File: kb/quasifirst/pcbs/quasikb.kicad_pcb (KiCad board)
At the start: 2 copper layers, 122.5 x 96.3 mm, 24 parts

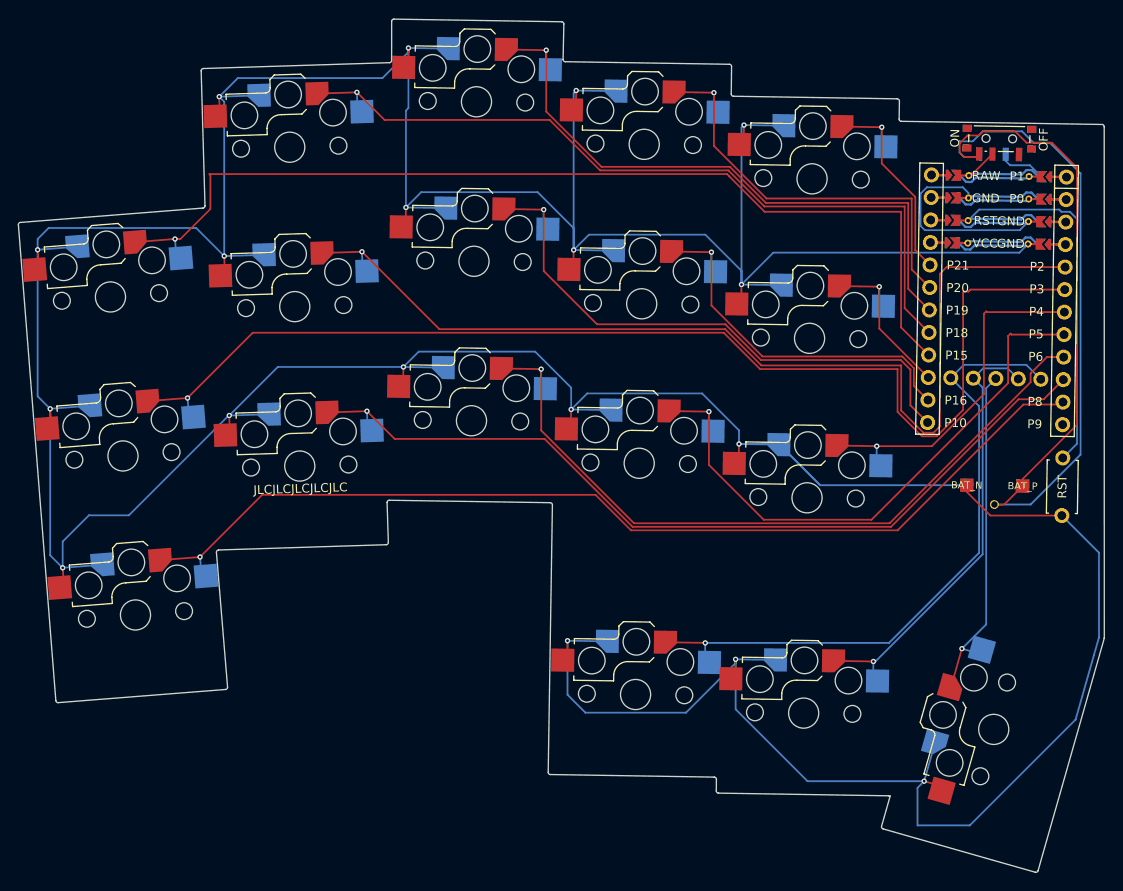
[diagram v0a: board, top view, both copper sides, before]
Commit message: finished routing, checked for issues, added eyesdropping
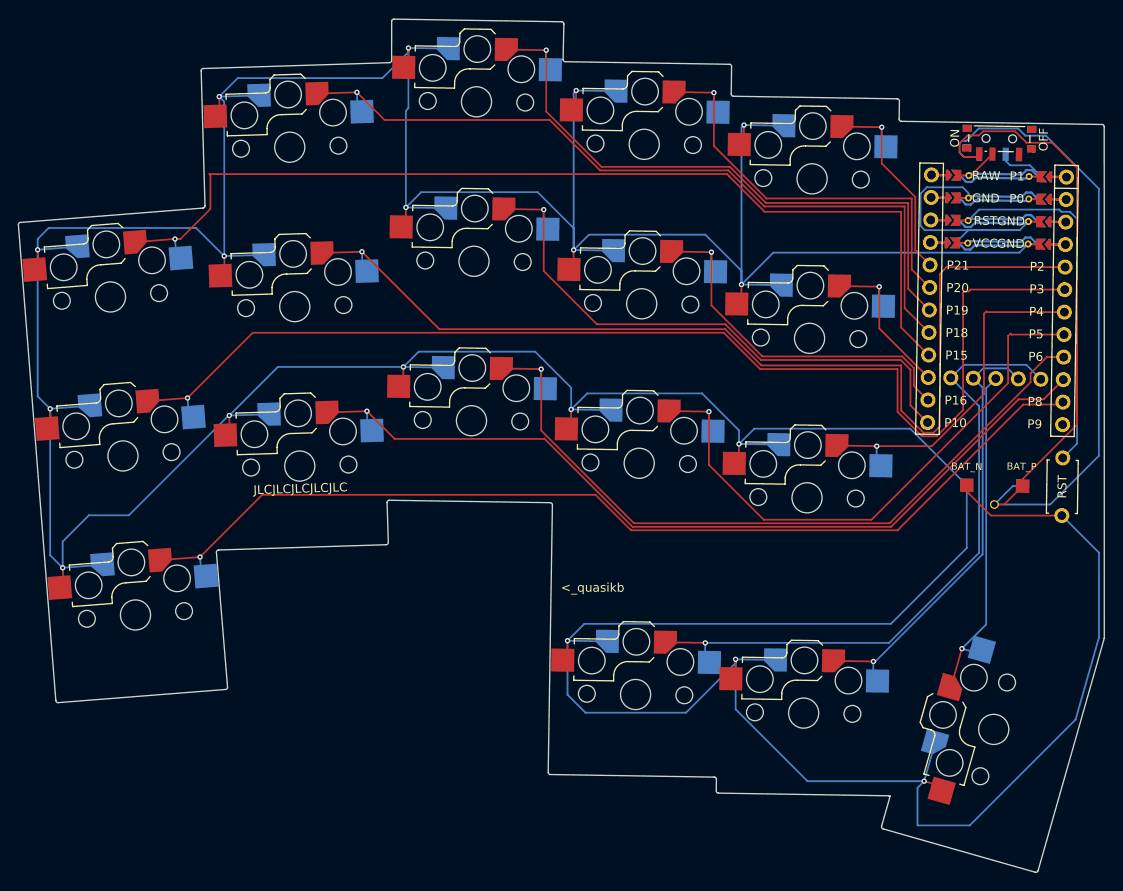
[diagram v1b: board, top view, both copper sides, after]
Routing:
- net GND: track 666.8 -> 731.9 mm
- net BAT_P: track 125.3 -> 132.7 mm
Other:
- board text added: "<_quasikb"

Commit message: adding ground area
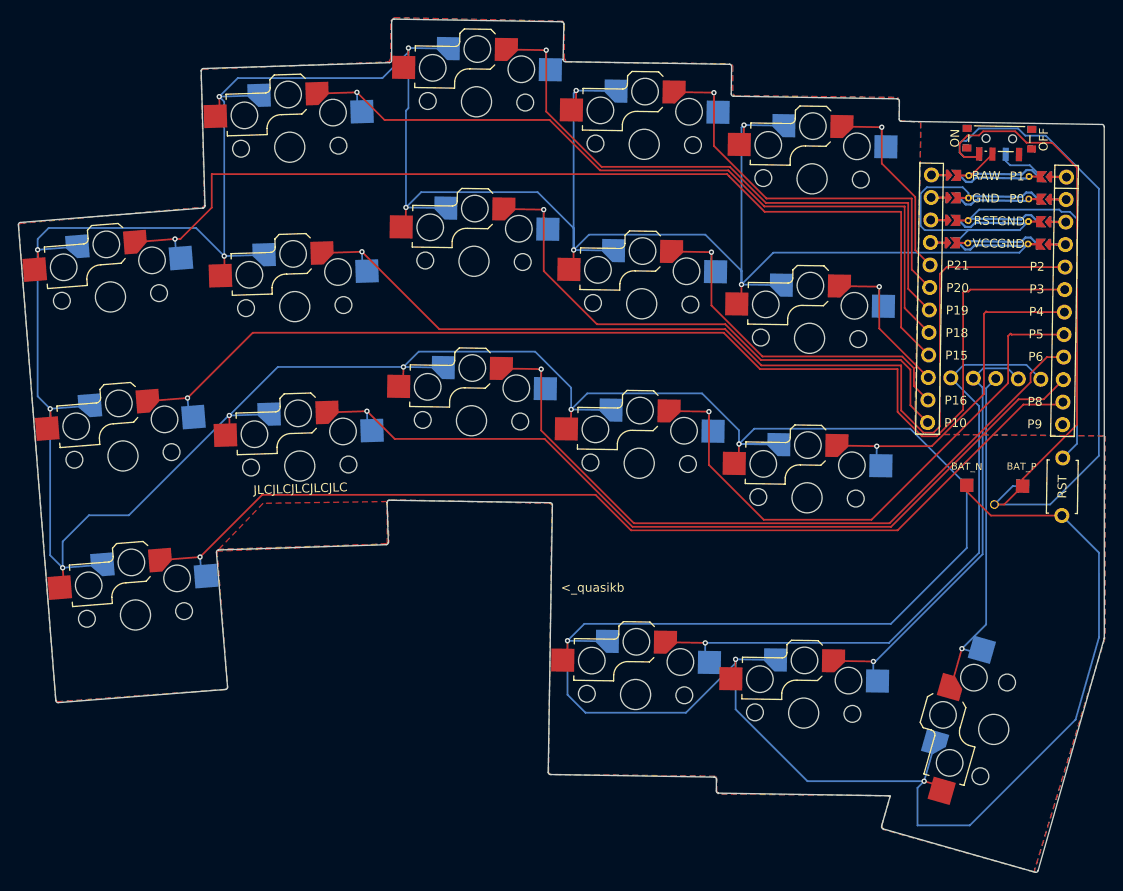
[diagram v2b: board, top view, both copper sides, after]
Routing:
- added copper zone on B.Cu, net GND
- added copper zone on F.Cu, net GND

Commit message: updating the kb signature
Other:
- board text added: ">_quasikb"
- board text removed: "<_quasikb"
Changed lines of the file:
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@@
 		(layer "Edge.Cuts")
 	)
-	(gr_text "<_quasikb"
+	(gr_text ">_quasikb"
 		(at 225.75 162.5 0)
 		(layer "B.SilkS")
@@
 			(justify left bottom mirror)
 		)
-		(render_cache "<_quasikb" 0
+		(render_cache ">_quasikb" 0
 			(polygon
 				(pts
-					(xy 225.081507 161.459762) (xy 224.996755 161.594096) (xy 225.47718 161.87986) (xy 224.996755 162.163426)
-					(xy 225.086636 162.299225) (xy 225.640823 161.953866) (xy 225.640823 161.805854)
+					(xy 225.555338 161.459762) (xy 224.996755 161.805122) (xy 224.996755 161.953866) (xy 225.551186 162.299225)
+					(xy 225.640823 162.167822) (xy 225.159909 161.87986) (xy 225.640823 161.597759)
 				)
 			)
@@
 		)
 	)
-	(gr_text "<_quasikb"
+	(gr_text ">_quasikb"
 		(at 218 162.5 0)
 		(layer "F.SilkS")
@@
 			(justify left bottom)
 		)
-		(render_cache "<_quasikb" 0
+		(render_cache ">_quasikb" 0
 			(polygon
 				(pts
-					(xy 218.668492 161.459762) (xy 218.753244 161.594096) (xy 218.272819 161.87986) (xy 218.753244 162.163426)
-					(xy 218.663363 162.299225) (xy 218.109176 161.953866) (xy 218.109176 161.805854)
+					(xy 218.194661 161.459762) (xy 218.753244 161.805122) (xy 218.753244 161.953866) (xy 218.198813 162.299225)
+					(xy 218.109176 162.167822) (xy 218.59009 161.87986) (xy 218.109176 161.597759)
 				)
 			)
